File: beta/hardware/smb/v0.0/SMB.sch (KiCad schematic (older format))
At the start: 21 parts, among them IC101 ATMEGA1284-A, J102 RTS_RESET, J103 ICSP, J104 SERIAL_REV, P101 I2C_CONN, SW101 reset_sw, X101 16MHz

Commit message: New layout almost done \o/
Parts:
- added P?: CONN_6, symbol CONN_6
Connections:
- net +5V: now also P?.1
- net /INT_I2C: now also P?.5
- net GND: now also P?.2
- net SCL: now also P?.3
- net SDA: now also P?.4
- no-connect marks 1 -> 2
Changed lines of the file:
@@
-EESchema Schematic File Version 2  date 23/07/2012 00:31:40
+EESchema Schematic File Version 2  date 29/07/2012 20:41:34
 LIBS:power
 LIBS:device
@@
 Sheet 1 4
 Title ""
-Date "22 jul 2012"
+Date "29 jul 2012"
 Rev ""
 Comp ""
@@
 $EndDescr
 Wire Wire Line
+	8400 4000 8400 4050
+Wire Wire Line
+	8400 4050 8250 4050
+Wire Wire Line
+	8250 4050 8250 3950
+Wire Wire Line
+	8700 4550 8700 4000
+Wire Wire Line
+	8500 4000 8500 4150
+Wire Wire Line
+	6600 5000 6550 5000
+Wire Wire Line
+	9450 4250 9550 4250
+Wire Wire Line
+	9550 4400 9450 4400
+Wire Wire Line
+	10350 4550 10350 4000
+Connection ~ 10350 4250
+Wire Wire Line
+	10050 4250 10350 4250
+Wire Wire Line
+	10050 4000 10050 4050
+Wire Wire Line
+	9900 4050 9900 3950
+Connection ~ 6800 3300
+Wire Wire Line
+	6800 3250 6800 3300
+Wire Wire Line
+	9950 3050 10050 3050
+Wire Wire Line
+	9950 3100 10050 3100
+Wire Wire Line
+	10200 3000 10200 3050
+Wire Wire Line
+	10200 3050 10100 3050
+Wire Wire Line
+	4550 2500 2650 2500
+Connection ~ 3350 3250
+Wire Wire Line
+	3300 3250 3350 3250
+Wire Notes Line
+	3500 2950 3500 3850
+Wire Notes Line
+	3500 2950 2500 2950
+Wire Notes Line
+	2500 2950 2500 3850
+Wire Wire Line
+	5250 5800 5250 5900
+Wire Wire Line
+	5450 5800 5450 5900
+Wire Wire Line
+	4850 1550 4850 1700
+Wire Wire Line
+	4350 1550 4350 1700
+Wire Wire Line
+	4100 1150 4100 1050
+Wire Wire Line
+	4100 1050 5350 1050
+Connection ~ 4850 1050
+Wire Wire Line
+	4850 1150 4850 1050
+Connection ~ 4350 1050
+Wire Wire Line
+	4350 1050 4350 1150
+Connection ~ 5450 1600
+Wire Wire Line
+	5650 1800 5650 1600
+Wire Wire Line
+	5650 1600 5250 1600
+Connection ~ 5350 1600
+Wire Wire Line
+	5250 1600 5250 1800
+Wire Notes Line
+	10950 3500 9300 3500
+Wire Wire Line
+	6600 4000 6550 4000
+Wire Wire Line
+	7100 2800 7100 2850
+Wire Wire Line
+	7200 3400 6550 3400
+Wire Wire Line
+	6600 4900 6550 4900
+Wire Wire Line
+	6600 3700 6550 3700
+Wire Wire Line
+	6600 3500 6550 3500
+Wire Wire Line
+	10400 5450 10400 5050
+Connection ~ 10600 5100
+Wire Wire Line
+	10600 5100 10550 5100
+Wire Wire Line
+	10550 5100 10550 5050
+Wire Wire Line
+	10350 5050 10350 5100
+Wire Wire Line
+	9950 5600 9950 5700
+Wire Wire Line
+	9950 5700 9550 5700
+Wire Wire Line
+	9850 5950 9850 6050
+Wire Wire Line
+	9650 5650 9650 5750
+Wire Wire Line
+	7750 5750 7750 5800
+Wire Wire Line
+	6550 5200 7300 5200
+Wire Wire Line
+	2650 3700 2650 3750
+Wire Wire Line
+	3350 3700 3350 3750
+Wire Notes Line
+	2500 3850 3500 3850
+Wire Wire Line
+	7700 5200 7750 5200
+Wire Wire Line
+	7750 5200 7750 5250
+Wire Wire Line
+	4500 2100 4550 2100
+Wire Wire Line
+	9650 5150 9650 5050
+Connection ~ 9650 5700
+Wire Wire Line
+	9950 5050 9950 5200
+Wire Wire Line
+	10000 5050 10000 5100
+Wire Wire Line
+	10000 5100 10350 5100
+Wire Wire Line
+	10600 5050 10600 5150
+Wire Wire Line
+	10500 5050 10500 5250
+Wire Wire Line
+	10500 5250 10850 5250
+Wire Wire Line
+	10850 5250 10850 5150
+Wire Wire Line
+	10450 5050 10450 5300
+Wire Wire Line
+	6600 3600 6550 3600
+Wire Wire Line
+	6600 4800 6550 4800
+Wire Wire Line
+	6600 5100 6550 5100
+Wire Wire Line
+	7100 3350 7100 3400
+Connection ~ 7100 3400
+Wire Notes Line
+	9300 4700 10950 4700
+Wire Notes Line
+	9300 6150 10950 6150
+Wire Wire Line
+	6600 3900 6550 3900
+Wire Wire Line
+	5350 1000 5350 1800
+Wire Wire Line
+	5450 1600 5450 1800
+Connection ~ 5350 1050
+Wire Wire Line
+	4600 1150 4600 1050
+Connection ~ 4600 1050
+Wire Wire Line
+	4100 1550 4100 1700
+Wire Wire Line
+	4600 1550 4600 1700
+Wire Wire Line
+	5550 5800 5550 5900
+Wire Wire Line
+	5350 5800 5350 5900
+Wire Wire Line
+	3350 3300 3350 2900
+Wire Wire Line
+	3350 2900 4550 2900
+Wire Wire Line
+	2650 3250 2700 3250
+Wire Wire Line
+	2650 2500 2650 3300
+Connection ~ 2650 3250
+Wire Wire Line
+	10100 3150 10200 3150
+Wire Wire Line
+	10200 3150 10200 3200
+Wire Wire Line
+	10200 3100 10100 3100
+Wire Wire Line
+	9950 3150 10050 3150
+Wire Notes Line
+	9300 6150 9300 2400
+Wire Notes Line
+	9300 2400 10950 2400
+Wire Notes Line
+	10950 2400 10950 6150
+Wire Wire Line
+	6850 3300 6550 3300
+Wire Wire Line
+	6800 2700 6800 2750
+Wire Wire Line
+	10150 4000 10150 4150
+Wire Wire Line
+	10250 4550 10250 4000
+Wire Wire Line
+	10050 4400 10250 4400
+Connection ~ 10250 4400
+Wire Wire Line
+	9450 4400 9450 4050
+Wire Wire Line
+	9450 4050 10050 4050
+Connection ~ 9900 4050
+Connection ~ 9450 4250
+Wire Wire Line
 	10450 4000 10450 4050
-Connection ~ 9450 4250
-Connection ~ 9900 4050
-Wire Wire Line
-	9450 4050 10050 4050
-Wire Wire Line
-	9450 4050 9450 4400
-Connection ~ 10250 4400
-Wire Wire Line
-	10050 4400 10250 4400
-Wire Wire Line
-	10250 4550 10250 4000
-Wire Wire Line
-	10150 4000 10150 4150
-Wire Wire Line
-	6800 2700 6800 2750
-Wire Wire Line
-	6850 3300 6550 3300
-Wire Notes Line
-	10950 2400 10950 6150
-Wire Notes Line
-	10950 2400 9300 2400
-Wire Notes Line
-	9300 2400 9300 6150
-Wire Wire Line
-	9950 3150 10050 3150
-Wire Wire Line
-	10200 3100 10100 3100
-Wire Wire Line
-	10200 3200 10200 3150
-Wire Wire Line
-	10200 3150 10100 3150
-Connection ~ 2650 3250
-Wire Wire Line
-	2650 3300 2650 2500
-Wire Wire Line
-	2650 3250 2700 3250
-Wire Wire Line
-	4550 2900 3350 2900
-Wire Wire Line
-	3350 2900 3350 3300
-Wire Wire Line
-	5350 5800 5350 5900
-Wire Wire Line
-	5550 5800 5550 5900
-Wire Wire Line
-	4600 1550 4600 1700
-Wire Wire Line
-	4100 1550 4100 1700
-Connection ~ 4600 1050
-Wire Wire Line
-	4600 1150 4600 1050
-Connection ~ 5350 1050
-Wire Wire Line
-	5450 1600 5450 1800
-Wire Wire Line
-	5350 1000 5350 1800
-Wire Wire Line
-	6600 3900 6550 3900
-Wire Notes Line
-	9300 6150 10950 6150
-Wire Notes Line
-	9300 4700 10950 4700
-Connection ~ 7100 3400
-Wire Wire Line
-	7100 3350 7100 3400
-Wire Wire Line
-	6600 5100 6550 5100
-Wire Wire Line
-	6600 4800 6550 4800
-Wire Wire Line
-	6600 3600 6550 3600
-Wire Wire Line
-	10450 5050 10450 5300
-Wire Wire Line
-	10850 5150 10850 5250
-Wire Wire Line
-	10850 5250 10500 5250
-Wire Wire Line
-	10500 5250 10500 5050
-Wire Wire Line
-	10600 5050 10600 5150
-Wire Wire Line
-	10000 5100 10350 5100
-Wire Wire Line
-	10000 5100 10000 5050
-Wire Wire Line
-	9950 5050 9950 5200
-Connection ~ 9650 5700
-Wire Wire Line
-	9650 5150 9650 5050
-Wire Wire Line
-	4500 2100 4550 2100
-Wire Wire Line
-	7750 5250 7750 5200
-Wire Wire Line
-	7750 5200 7700 5200
-Wire Notes Line
-	2500 3850 3500 3850
-Wire Wire Line
-	3350 3700 3350 3750
-Wire Wire Line
-	2650 3700 2650 3750
-Wire Wire Line
-	6550 5200 7300 5200
-Wire Wire Line
-	7750 5750 7750 5800
-Wire Wire Line
-	9650 5650 9650 5750
-Wire Wire Line
-	9850 5950 9850 6050
-Wire Wire Line
-	9550 5700 9950 5700
-Wire Wire Line
-	9950 5700 9950 5600
-Wire Wire Line
-	10350 5100 10350 5050
-Wire Wire Line
-	10550 5050 10550 5100
-Wire Wire Line
-	10550 5100 10600 5100
-Connection ~ 10600 5100
-Wire Wire Line
-	10400 5450 10400 5050
-Wire Wire Line
-	6600 3500 6550 3500
-Wire Wire Line
-	6600 3700 6550 3700
-Wire Wire Line
-	6600 4900 6550 4900
-Wire Wire Line
-	7200 3400 6550 3400
-Wire Wire Line
-	7100 2800 7100 2850
-Wire Wire Line
-	6600 4000 6550 4000
-Wire Notes Line
-	10950 3500 9300 3500
-Wire Wire Line
-	5250 1800 5250 1600
-Connection ~ 5350 1600
-Wire Wire Line
-	5250 1600 5650 1600
-Wire Wire Line
-	5650 1600 5650 1800
-Connection ~ 5450 1600
-Wire Wire Line
-	4350 1050 4350 1150
-Connection ~ 4350 1050
-Wire Wire Line
-	4850 1150 4850 1050
-Connection ~ 4850 1050
-Wire Wire Line
-	5350 1050 4100 1050
-Wire Wire Line
-	4100 1050 4100 1150
-Wire Wire Line
-	4350 1550 4350 1700
-Wire Wire Line
-	4850 1550 4850 1700
-Wire Wire Line
-	5450 5800 5450 5900
-Wire Wire Line
-	5250 5800 5250 5900
-Wire Notes Line
-	2500 3850 2500 2950
-Wire Notes Line
-	2500 2950 3500 2950
-Wire Notes Line
-	3500 2950 3500 3850
-Wire Wire Line
-	3300 3250 3350 3250
-Connection ~ 3350 3250
-Wire Wire Line
-	2650 2500 4550 2500
-Wire Wire Line
-	10100 3050 10200 3050
-Wire Wire Line
-	10200 3050 10200 3000
-Wire Wire Line
-	9950 3100 10050 3100
-Wire Wire Line
-	9950 3050 10050 3050
-Wire Wire Line
-	6800 3250 6800 3300
-Connection ~ 6800 3300
-Wire Wire Line
-	9900 4050 9900 3950
-Wire Wire Line
-	10050 4050 10050 4000
-Wire Wire Line
-	10050 4250 10350 4250
-Connection ~ 10350 4250
-Wire Wire Line
-	10350 4550 10350 4000
-Wire Wire Line
-	9450 4400 9550 4400
-Wire Wire Line
-	9450 4250 9550 4250
-Wire Wire Line
-	6600 5000 6550 5000
+Wire Wire Line
+	8800 4000 8800 4050
+Wire Wire Line
+	8600 4000 8600 4550
+$Comp
+L +5V #PWR?
+U 1 1 501583C6
+P 8250 3950
+F 0 "#PWR?" H 8250 4040 20  0001 C CNN
+F 1 "+5V" H 8250 4040 30  0000 C CNN
+	1    8250 3950
+	1    0    0    -1
+$EndComp
+Text GLabel 8600 4550 3    25   BiDi ~ 0
+SCL
+Text GLabel 8700 4550 3    25   BiDi ~ 0
+SDA
+Text GLabel 8800 4050 3    25   Output ~ 0
+/INT_I2C
+$Comp
+L GND #PWR?
+U 1 1 5015827B
+P 8500 4150
+F 0 "#PWR?" H 8500 4150 30  0001 C CNN
+F 1 "GND" H 8500 4080 30  0001 C CNN
+	1    8500 4150
+	1    0    0    -1
+$EndComp
+NoConn ~ 8900 4000
+$Comp
+L CONN_6 P?
+U 1 1 50158246
+P 8650 3650
+F 0 "P?" V 8600 3650 60  0000 C CNN
+F 1 "CONN_6" V 8700 3650 60  0000 C CNN
+	1    8650 3650
+	0    -1   -1   0
+$EndComp
 Text GLabel 10450 4050 3    25   Output ~ 0
 /INT_I2C

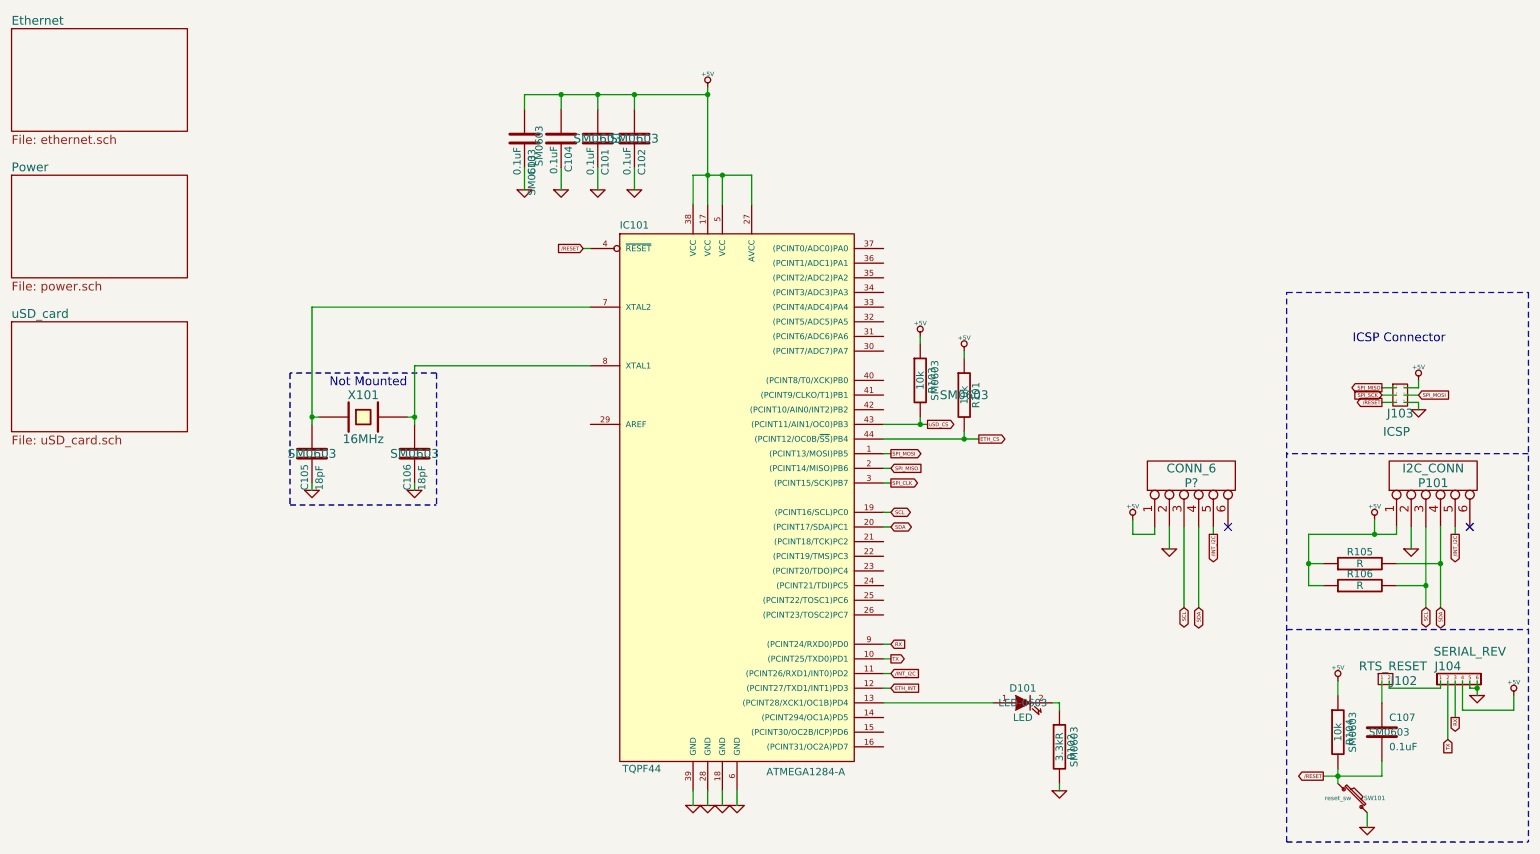
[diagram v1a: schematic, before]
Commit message: Added JTAG and ADC Port
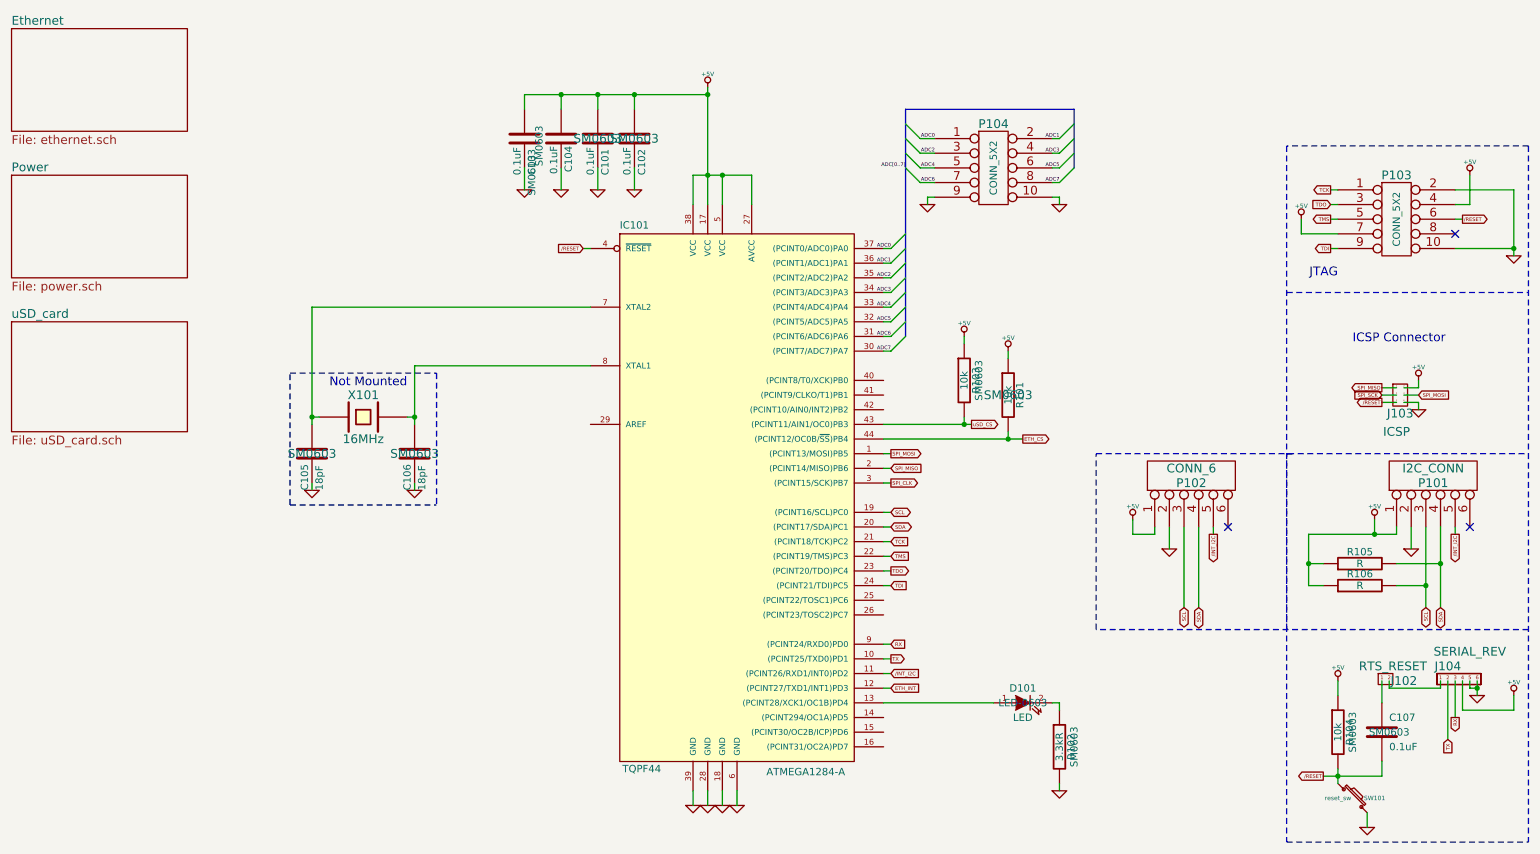
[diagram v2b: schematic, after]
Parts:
- added P103, P104: CONN_5X2, symbol CONN_5X2
- gave numbers to parts that had none: 1
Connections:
- net +5V: now also P103.4, P103.7
- net /RESET: now also P103.6
- net GND: now also P103.10, P103.2, P104.10, P104.9
- net TCK: now reaches IC101.21 ((PCINT18/TCK)PC2)
- net TCK: now also P103.1
- net TMS: now reaches IC101.22 ((PCINT19/TMS)PC3)
- net TMS: now also P103.5
- net TDO: now reaches IC101.23 ((PCINT20/TDO)PC4)
- net TDO: now also P103.3
- net TDI: now reaches IC101.24 ((PCINT21/TDI)PC5)
- net TDI: now also P103.9
- net ADC7: now reaches IC101.30 ((PCINT7/ADC7)PA7)
- net ADC7: now also P104.8
- net ADC6: now reaches IC101.31 ((PCINT6/ADC6)PA6)
- net ADC6: now also P104.7
- net ADC5: now reaches IC101.32 ((PCINT5/ADC5)PA5)
- net ADC5: now also P104.6
- net ADC4: now reaches IC101.33 ((PCINT4/ADC4)PA4)
- net ADC4: now also P104.5
- net ADC3: now reaches IC101.34 ((PCINT3/ADC3)PA3)
- net ADC3: now also P104.4
- net ADC2: now reaches IC101.35 ((PCINT2/ADC2)PA2)
- net ADC2: now also P104.3
- net ADC1: now reaches IC101.36 ((PCINT1/ADC1)PA1)
- net ADC1: now also P104.2
- net ADC0: now reaches IC101.37 ((PCINT0/ADC0)PA0)
- net ADC0: now also P104.1
- no-connect marks 2 -> 3
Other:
- note added: "JTAG"
- moved on the sheet: R101, R103
